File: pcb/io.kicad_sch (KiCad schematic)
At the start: 0 parts

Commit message: add the din connector
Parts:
- added J?: 650913-5, TE_650913-5, symbol 650913-5:650913-5
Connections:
- new net DIN1: J?.1
- new net DIN10: J?.10
- new net DIN11: J?.11
- new net DIN12: J?.12
- new net DIN13: J?.13
- new net DIN14: J?.14
- new net DIN15: J?.15
- new net DIN16: J?.16
- new net DIN17: J?.17
- new net DIN18: J?.18
- new net DIN2: J?.2
- new net DIN20: J?.20
- new net DIN21: J?.21
- new net DIN22: J?.22
- new net DIN23: J?.23
- new net DIN24: J?.24
- new net DIN25: J?.25
- new net DIN26: J?.26
- new net DIN27: J?.27
- new net DIN28: J?.28
- new net DIN29: J?.29
- new net DIN3: J?.3
- new net DIN30: J?.30
- new net DIN31: J?.31
- new net DIN32: J?.32
- new net DIN34: J?.34
- new net DIN35: J?.35
- new net DIN37: J?.37
- new net DIN38: J?.38
- new net DIN4: J?.4
- new net DIN40: J?.40
- new net DIN41: J?.41
- new net DIN43: J?.43
- new net DIN44: J?.44
- new net DIN46: J?.46
- new net DIN47: J?.47
- new net DIN49: J?.49
- new net DIN5: J?.5
- new net DIN50: J?.50
- new net DIN52: J?.52
- new net DIN53: J?.53
- new net DIN55: J?.55
- new net DIN56: J?.56
- new net DIN58: J?.58
- new net DIN59: J?.59
- new net DIN61: J?.61
- new net DIN62: J?.62
- new net DIN64: J?.64
- new net DIN65: J?.65
- new net DIN66: J?.66
- new net DIN67: J?.67
- new net DIN68: J?.68
- new net DIN69: J?.69
- new net DIN7: J?.7
- new net DIN70: J?.70
- new net DIN71: J?.71
- new net DIN72: J?.72
- new net DIN73: J?.73
- new net DIN74: J?.74
- new net DIN75: J?.75
- new net DIN77: J?.77
- new net DIN78: J?.78
- new net DIN79: J?.79
- new net DIN8: J?.8
- new net DIN80: J?.80
- new net DIN81: J?.81
- new net DIN82: J?.82
- new net DIN83: J?.83
- new net DIN84: J?.84
- new net DIN85: J?.85
- new net DIN86: J?.86
- new net DIN87: J?.87
- new net DIN88: J?.88
- new net DIN9: J?.9
- new net DIN90: J?.90
- new net DIN91: J?.91
- new net DIN92: J?.92
- new net DIN93: J?.93
- new net DIN94: J?.94
- new net DIN95: J?.95
- new net DIN96: J?.96
- new net GND: J?.33, J?.36, J?.39, J?.42, J?.45, J?.48, J?.51, J?.54, J?.57, J?.60, J?.63
- new net VCC: J?.19, J?.6, J?.76, J?.89
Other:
- note added: "Ground pins are placed in the middle so that each signal pin is next to a ground pin, including diagonaly."
- note added: "The maximum power is 30W. This means 2.5A at 12V. Each pin is rated at 2A. We will use 4 pins for a maximum 625mA per pin"

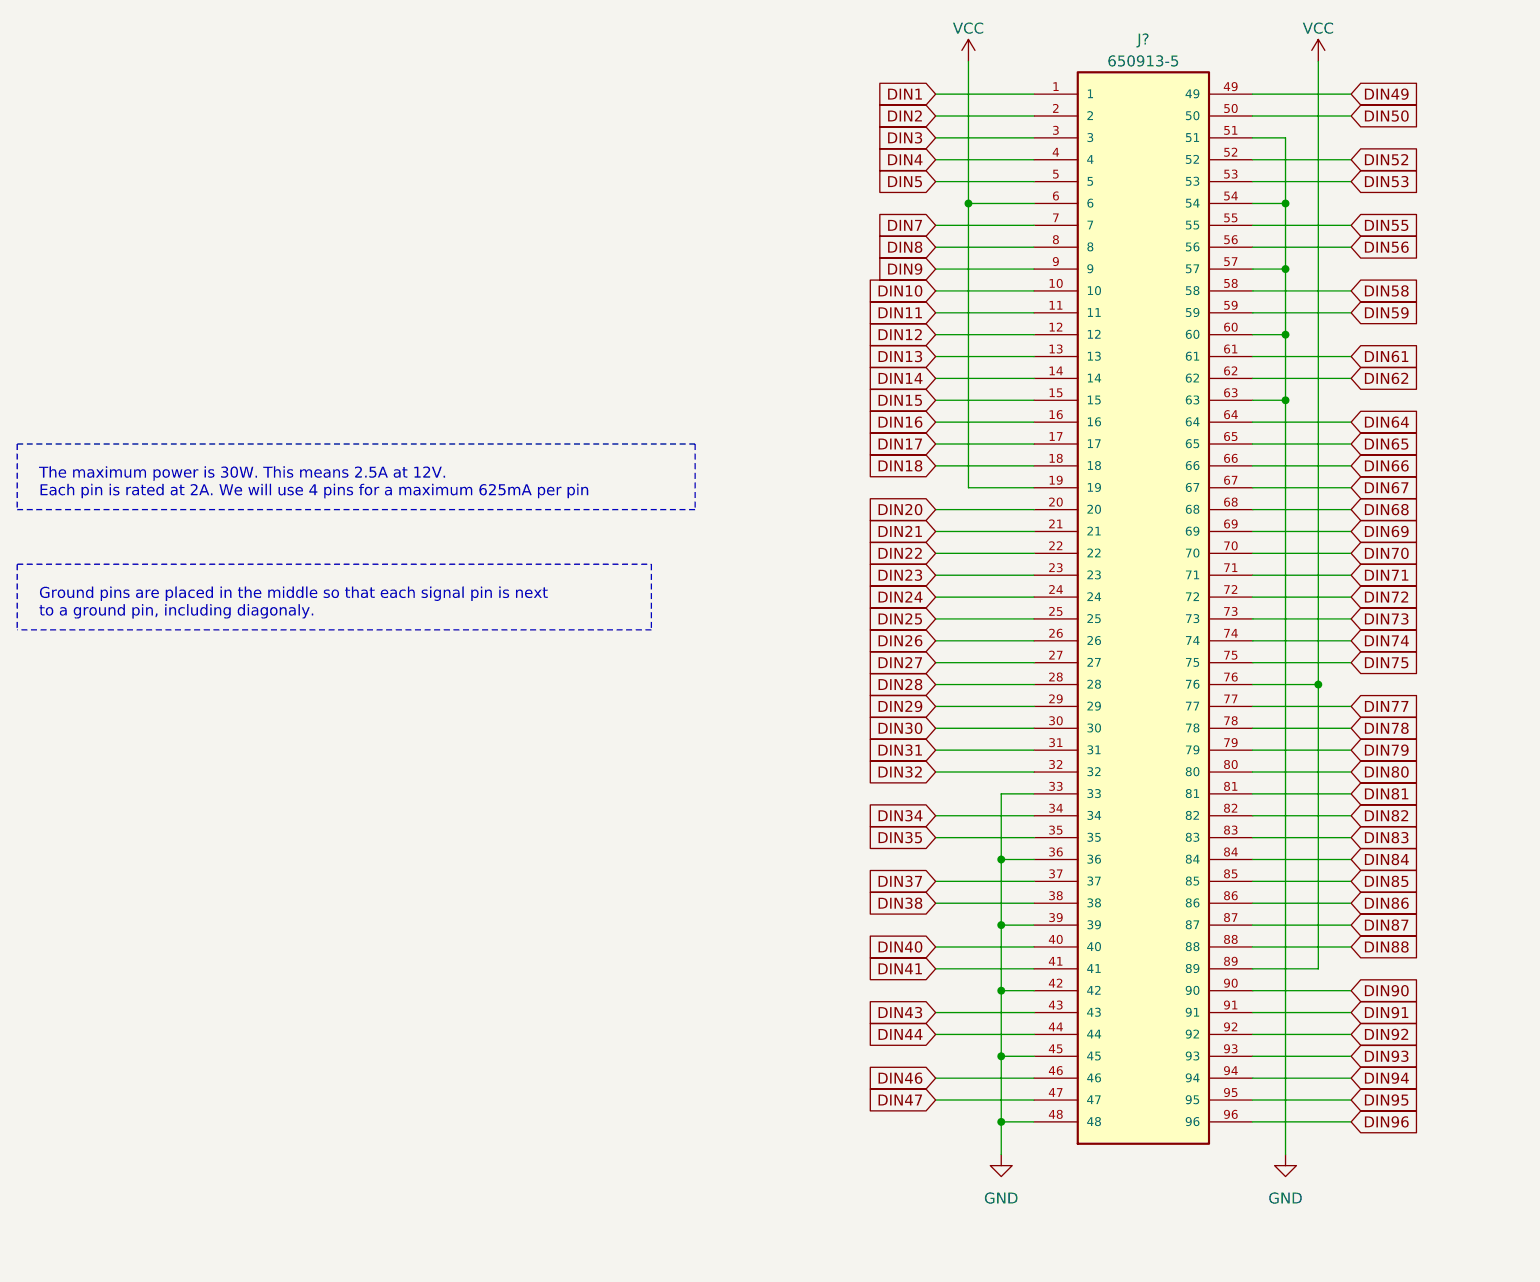
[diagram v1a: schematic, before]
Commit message: start associating footprints
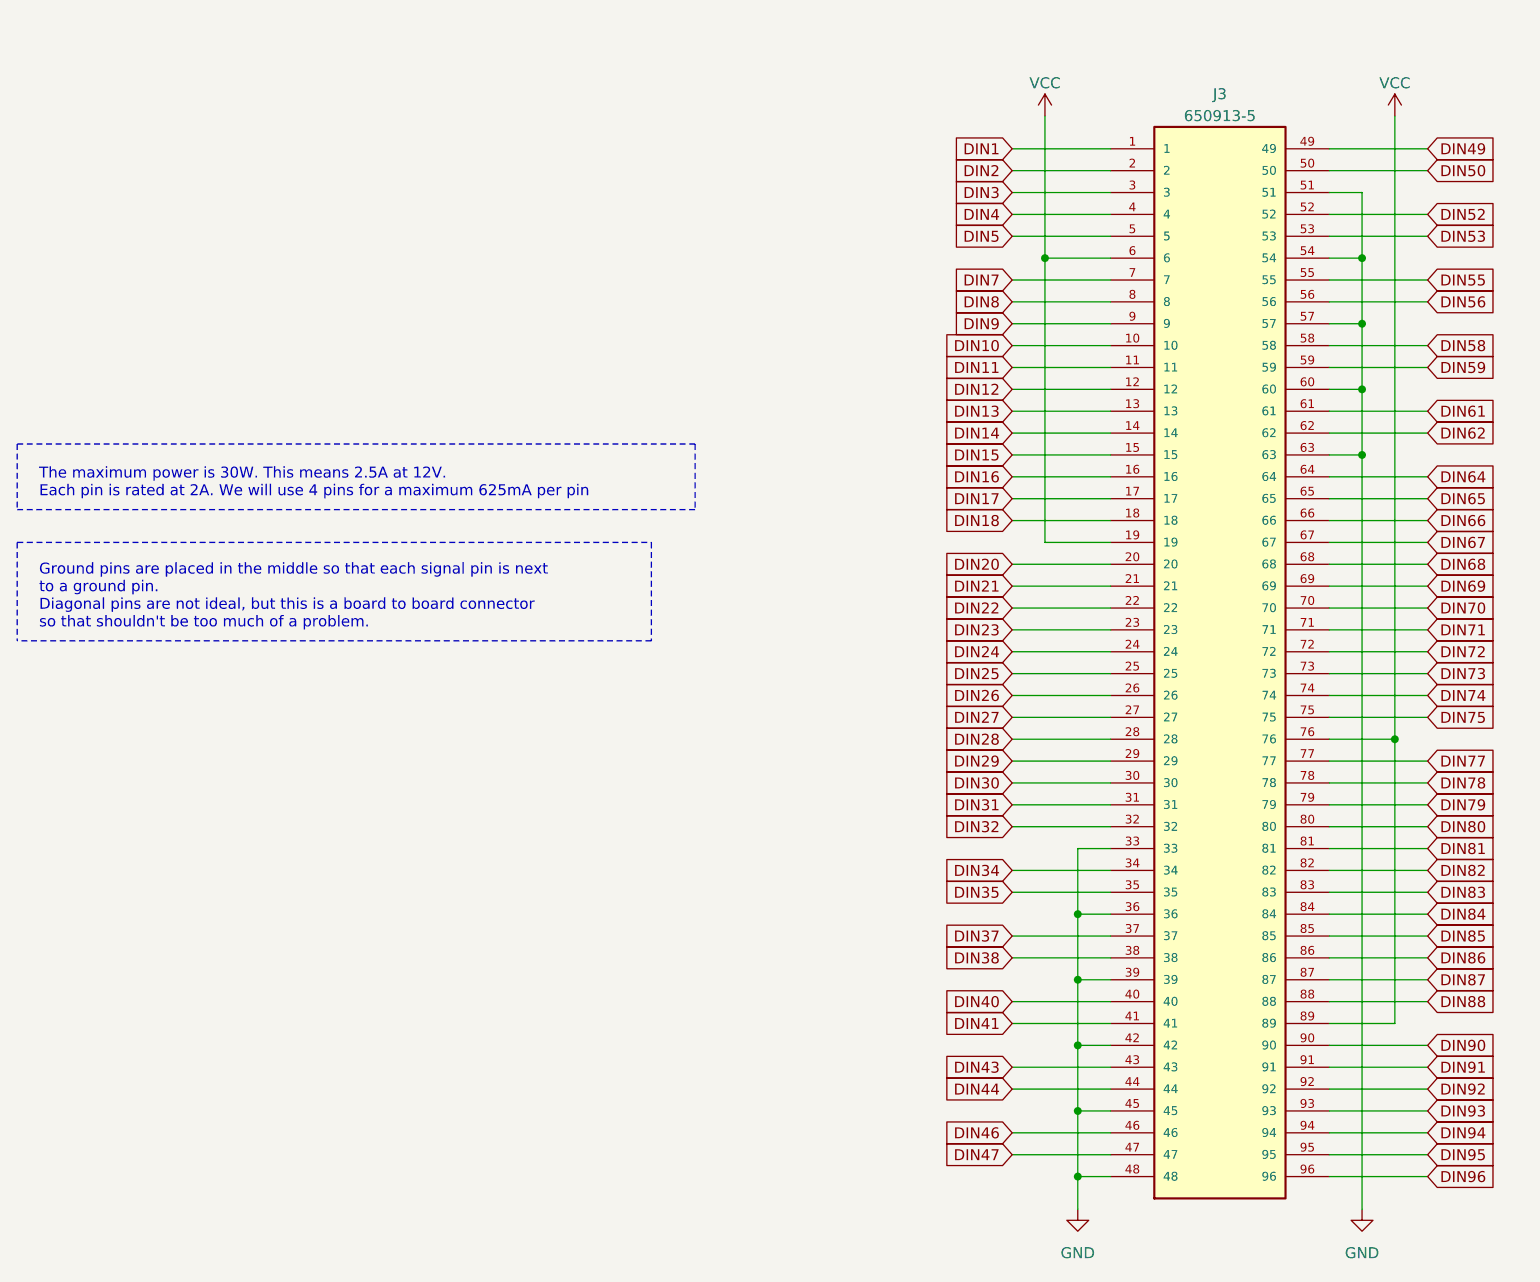
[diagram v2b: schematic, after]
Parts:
- J3: renamed from J?; footprint TE_650913-5 -> (none)
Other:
- note added: "Ground pins are placed in the middle so that each signal pin is next to a ground pin. Diagonal pins are not ideal, but this is a board to board connector so that shouldn't be too much of a problem."
- note removed: "Ground pins are placed in the middle so that each signal pin is next to a ground pin, including diagonaly."
- moved on the sheet: J3

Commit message: add tps541620 footprint
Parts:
- J3: footprint (none) -> Connector_DIN:TE_650913-5
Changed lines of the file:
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@@
     (property "Reference" "J3" (id 0) (at 167.64 26.67 0))
     (property "Value" "650913-5" (id 1) (at 167.64 29.21 0))
-    (property "Footprint" "" (id 2) (at 167.64 93.98 0)
+    (property "Footprint" "Connector_DIN:TE_650913-5" (id 2) (at 167.64 93.98 0)
       (effects (font (size 1.27 1.27)) (justify left bottom) hide)
     )

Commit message: add components to pcb
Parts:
- J3: footprint Connector_DIN:TE_650913-5 -> 650913-5:TE_650913-5
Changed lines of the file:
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@@
-(kicad_sch (version 20210126) (generator eeschema)
+(kicad_sch (version 20210406) (generator eeschema)
   (paper "User" 240.005 200)
   (junction (at 147.32 45.72) (diameter 0.9144) (color 0 0 0 0))
@@
     (property "Reference" "J3" (id 0) (at 167.64 26.67 0))
     (property "Value" "650913-5" (id 1) (at 167.64 29.21 0))
-    (property "Footprint" "Connector_DIN:TE_650913-5" (id 2) (at 167.64 93.98 0)
+    (property "Footprint" "650913-5:TE_650913-5" (id 2) (at 167.64 93.98 0)
       (effects (font (size 1.27 1.27)) (justify left bottom) hide)
     )

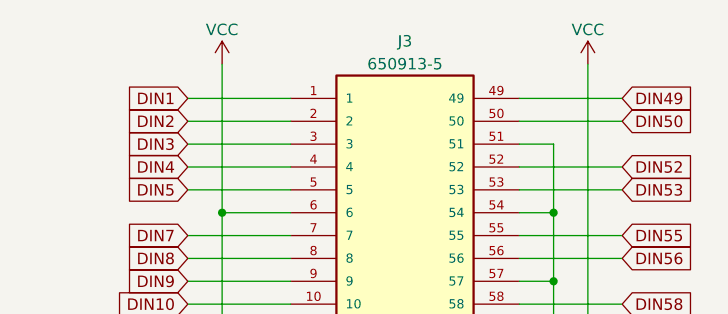
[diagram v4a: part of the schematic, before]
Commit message: route pol
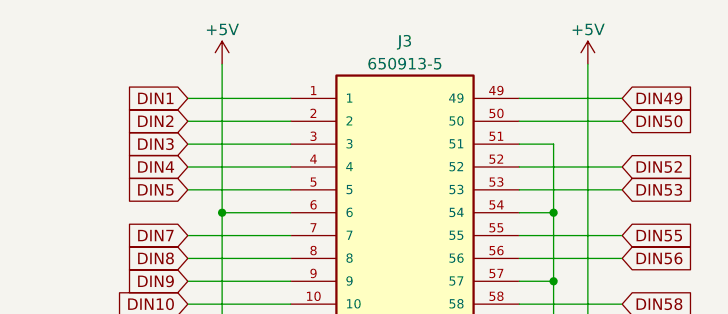
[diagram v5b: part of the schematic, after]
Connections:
- net VCC renamed +5V
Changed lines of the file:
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@@
     )
   )
-  (symbol (lib_id "power:VCC") (at 147.32 29.21 0) (unit 1)
+  (symbol (lib_id "power:+5V") (at 147.32 29.21 0) (unit 1)
     (in_bom yes) (on_board yes) (fields_autoplaced)
-    (property "Reference" "#PWR083" (id 0) (at 147.32 33.02 0)
+    (property "Reference" "#PWR0135" (id 0) (at 147.32 33.02 0)
       (effects (font (size 1.27 1.27)) hide)
     )
-    (property "Value" "VCC" (id 1) (at 147.32 25.4 0))
+    (property "Value" "+5V" (id 1) (at 147.32 25.4 0))
     (property "Footprint" "" (id 2) (at 147.32 29.21 0)
       (effects (font (size 1.27 1.27)) hide)
@@
     (pin "1")
   )
-  (symbol (lib_id "power:VCC") (at 187.96 29.21 0) (unit 1)
+  (symbol (lib_id "power:+5V") (at 187.96 29.21 0) (unit 1)
     (in_bom yes) (on_board yes) (fields_autoplaced)
-    (property "Reference" "#PWR084" (id 0) (at 187.96 33.02 0)
+    (property "Reference" "#PWR0136" (id 0) (at 187.96 33.02 0)
       (effects (font (size 1.27 1.27)) hide)
     )
-    (property "Value" "VCC" (id 1) (at 187.96 25.4 0))
+    (property "Value" "+5V" (id 1) (at 187.96 25.4 0))
     (property "Footprint" "" (id 2) (at 187.96 29.21 0)
       (effects (font (size 1.27 1.27)) hide)
